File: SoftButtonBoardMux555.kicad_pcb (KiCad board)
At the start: 2 copper layers, 26.4 x 22 mm, 19 parts, among them J1 IN_OUT, J2 SW, J3 EFF_IN_OUT, J4 PWR_IN, U1 NE555DR, U2 TPS76950, U3 ADG884BRMZ, U4 ADG884BRMZ

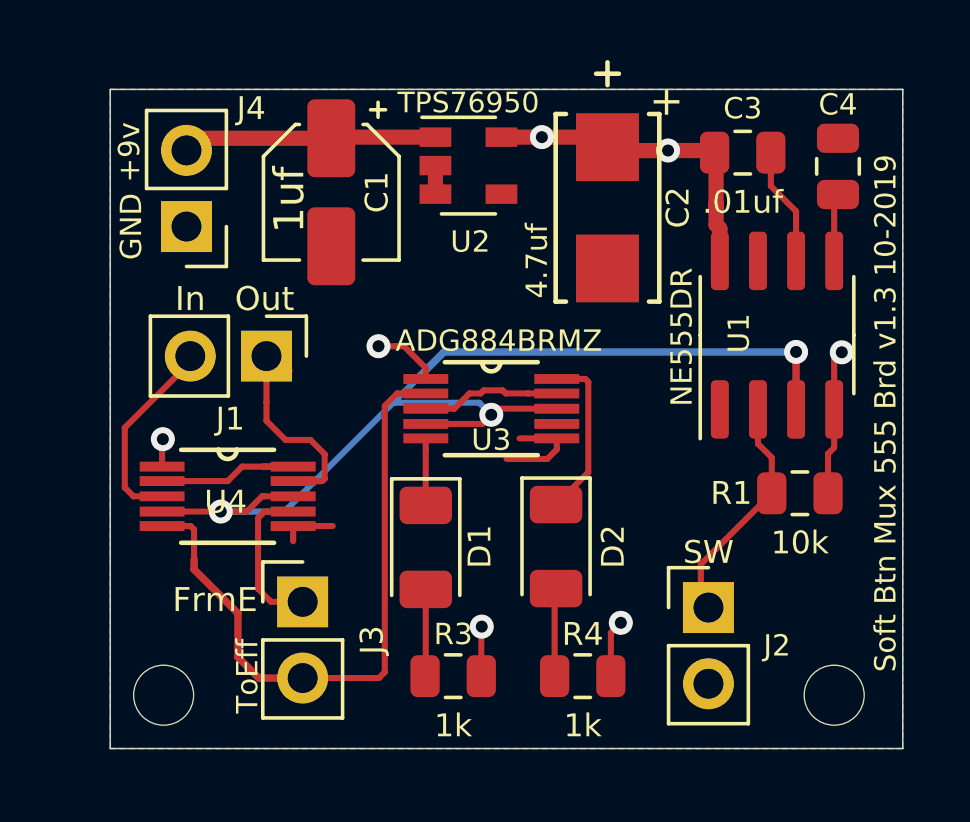
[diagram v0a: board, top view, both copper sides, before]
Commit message: fix switch connection
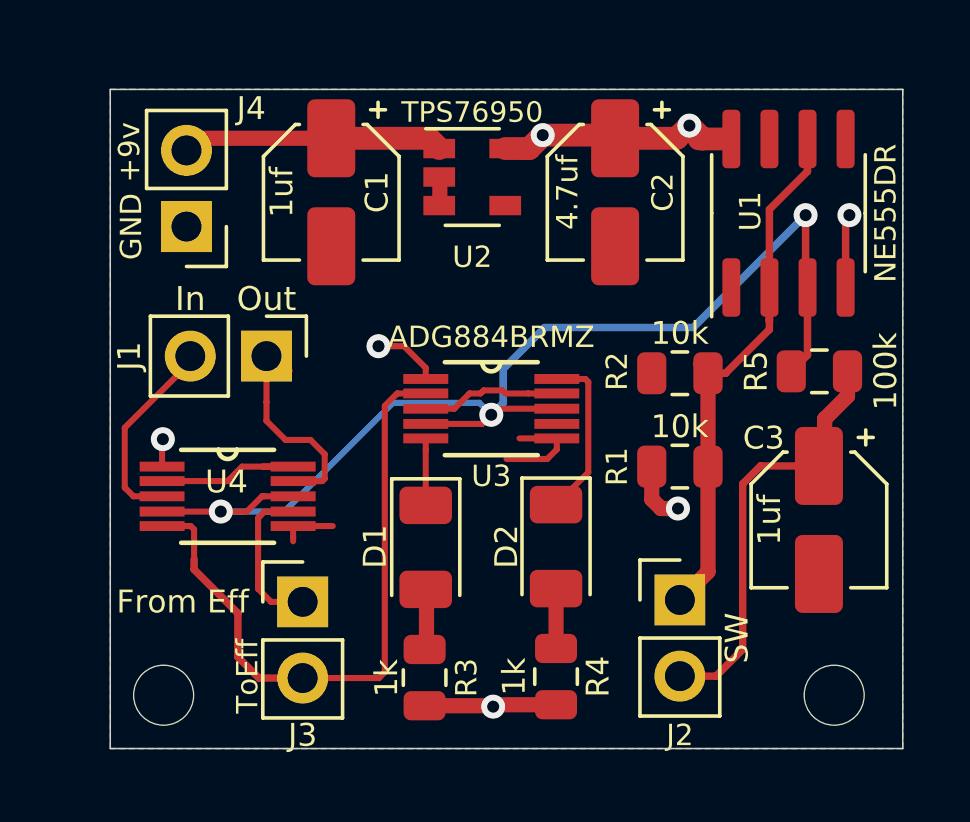
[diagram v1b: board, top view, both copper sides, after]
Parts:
- removed C4: .01uf, Capacitor_SMD:C_0805_2012Metric
- added R2: 10k, Resistor_SMD:R_0805_2012Metric, F.Cu at (96.7, 53.3)
- added R5: 100k, Resistor_SMD:R_0805_2012Metric, F.Cu at (101.4, 53.2)
- C2: footprint TPSC475K035R0600:TPSC475K035R0600 -> Capacitor_SMD:CP_Elec_4x3.9
- C3: value .01uf -> 1uf; footprint Capacitor_SMD:C_0805_2012Metric -> Capacitor_SMD:CP_Elec_4x3.9
- moved C3 12.5 mm to (101.3, 58.2), turned to 270 degrees
- moved R1 4.10 mm to (96.7, 56.4), turned to 180 degrees
- moved U1 4.08 mm to (100.3, 47.9)
- moved J2 0.99 mm to (96.7, 60.8)
- moved R3 0.95 mm to (88.2, 63.4), turned to 270 degrees
- moved R4 0.89 mm to (92.6, 63.4), turned to 270 degrees
- moved C2 0.58 mm to (94.6, 47.2)
- moved U2 0.40 mm to (89.8, 46.7)
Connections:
- C3 pad 1: Vcc -> Net-(C3-Pad1)
- C3 pad 2: Net-(C3-Pad2) -> GND
- J2 pad 2: GND -> Net-(C3-Pad1)
- U1 pad 6: Net-(C3-Pad2) -> Net-(J2-Pad1)
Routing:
- net Net-(C3-Pad1): track 0.00 -> 14.2 mm
- net Net-(J2-Pad1): track 7.78 -> 19.2 mm
- net Net-(C3-Pad2): track 3.96 -> 0.00 mm
- net ON_SIG: track 36.8 -> 39.2 mm
- net Net-(U1-Pad5): track 2.27 -> 0.00 mm
- net Vcc: track 23.0 -> 21.2 mm
- net Net-(D2-Pad2): track 2.94 -> 2.00 mm
- net Net-(D1-Pad2): track 2.90 -> 2.05 mm
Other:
- board text added: "From Eff"
- board text added: "Soft Btn Mux 555 v1.4 11-2019"
- board text removed: "+"
- board text removed: "FrmE"
- board text removed: "Soft Btn Mux 555 Brd v1.3 10-2019"

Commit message: Switch to new LDO reduce the size and add better connection points
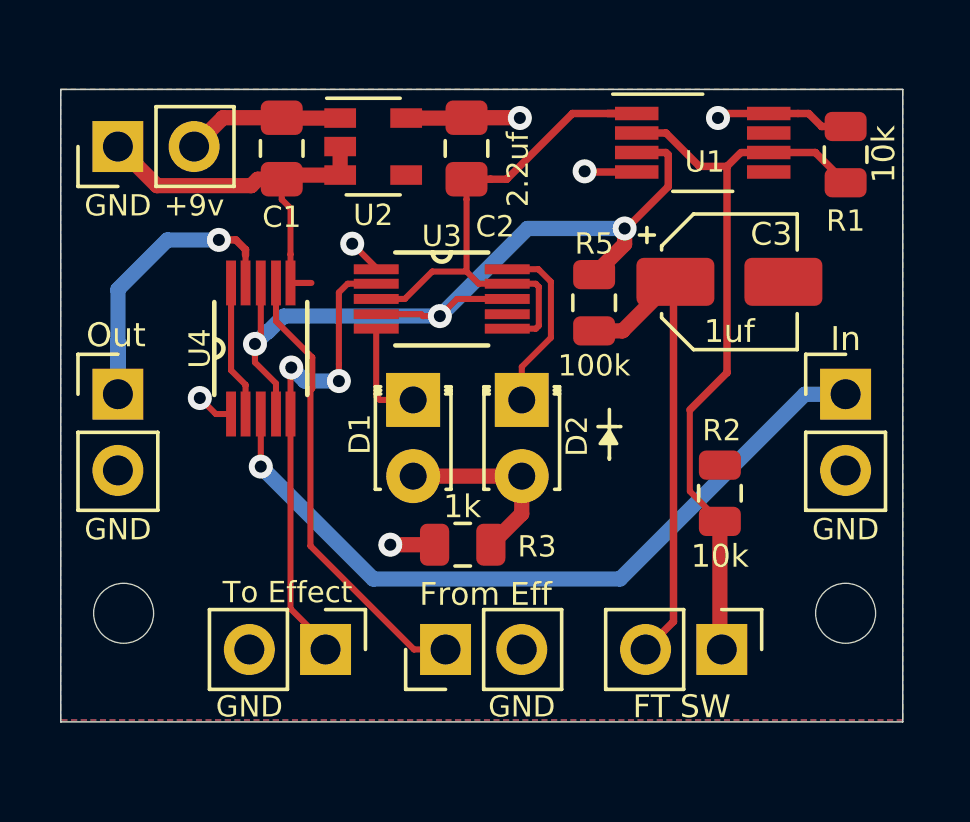
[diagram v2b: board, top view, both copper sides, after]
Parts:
- removed R4: 1k, Resistor_SMD:R_0805_2012Metric
- added J5: IN_OUT, Connector_PinHeader_2.54mm:PinHeader_1x02_P2.54mm_Vertical, F.Cu at (102.2, 54.0)
- added J6: EFF_IN_OUT, Connector_PinHeader_2.54mm:PinHeader_1x02_P2.54mm_Vertical, F.Cu at (84.9, 62.5)
- C1: footprint Capacitor_SMD:CP_Elec_4x3.9 -> Capacitor_SMD:C_0805_2012Metric_Pad1.15x1.40mm_HandSolder
- C2: value 4.7uf -> 2.2uf; footprint Capacitor_SMD:CP_Elec_4x3.9 -> Capacitor_SMD:C_0805_2012Metric_Pad1.15x1.40mm_HandSolder
- D1, D2: footprint LED_SMD:LED_1206_3216Metric -> LED_THT:LED_D1.8mm_W3.3mm_H2.4mm
- J2: value SW -> FT SW
- U1: footprint Package_SO:SOIC-8_3.9x4.9mm_P1.27mm -> Package_SO:VSSOP-8_3.0x3.0mm_P0.65mm
- U2: value TPS76950 -> AP2204K-5.0
- moved R1 11.8 mm to (102.2, 46.0), turned to 90 degrees
- moved C3 8.48 mm to (98.4, 50.2), turned to 0 degrees
- moved R5 7.85 mm to (93.9, 50.9), turned to 270 degrees
- moved C2 5.16 mm to (89.6, 45.8)
- moved J1 5.11 mm to (78.0, 54.0), turned to 0 degrees
- moved U4 5.05 mm to (82.7, 52.5), turned to 90 degrees
- moved D2 5.02 mm to (91.4, 54.2)
- moved J3 5.02 mm to (88.9, 62.5), turned to 90 degrees
- moved D1 4.93 mm to (87.8, 54.2)
- moved R3 4.61 mm to (89.5, 59.0), turned to 180 degrees
- moved R2 4.22 mm to (98.0, 57.3), turned to 90 degrees
- moved U3 4.01 mm to (88.8, 50.8)
- moved U1 3.70 mm to (97.5, 45.6), turned to 0 degrees
- moved J4 3.51 mm to (78.0, 45.7), turned to 90 degrees
- moved U2 3.45 mm to (86.5, 45.7)
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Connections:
- D2 pad 2: Net-(D2-Pad2) -> Net-(D1-Pad2)
- J1 pad 2: Input -> GND
- J3 pad 2: ToEffect -> GND
- U1 pad 5: Net-(U1-Pad5) -> (no net)
- U1 pad 7: Net-(U1-Pad7) -> (no net)
- U2 pad 4: Net-(U2-Pad4) -> (no net)
- U3 pad 7: Net-(U3-Pad7) -> (no net)
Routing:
- net GND: track 10.9 -> 33.1 mm
- net Input: track 6.05 -> 26.4 mm, vias 0 -> 1
- net FromEffect: track 5.28 -> 15.2 mm
- net ON_SIG: track 39.2 -> 29.5 mm
- net Net-(J2-Pad1): track 19.2 -> 27.1 mm
- net Vcc: track 21.2 -> 14.0 mm, vias 7 -> 6
- net ToEffect: track 21.7 -> 16.1 mm, vias 0 -> 2
- net Output: track 7.99 -> 12.6 mm, vias 0 -> 1
- net Net-(D1-Pad2): track 2.05 -> 6.33 mm
- net +9V: track 8.28 -> 5.27 mm
- net Net-(D2-Pad2): track 2.00 -> 0.00 mm
- net Net-(C3-Pad1): track 14.2 -> 16.1 mm
- net Net-(D1-Pad1): track 2.23 -> 3.53 mm
- net Net-(U4-Pad10): track 5.62 -> 4.57 mm
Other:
- board size 26.4 x 22 mm -> 28.1 x 21.1 mm
- board text added: "Soft Btn Mux 555 v2.0 11-2019"
- board text added: "To Effect"
- board text removed: "Soft Btn Mux 555 v1.4 11-2019"
- board text removed: "ToEff"
